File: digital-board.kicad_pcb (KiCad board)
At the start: 2 copper layers, 200 x 150 mm, 231 parts, among them IC1 ATMEGA6450-A, J1 CONN_20X2, Q1 2N3904, Q2 2N3904, SW15 TACT_SWITCH, SW16 TACT_SWITCH, SW17 TACT_SWITCH, SW18 TACT_SWITCH, SW19 TACT_SWITCH, SW20 TACT_SWITCH, SW21 TACT_SWITCH, SW22 TACT_SWITCH, SW23 TACT_SWITCH, U1 DG419, U10 74LVC1G32, U12 74AC595, U13 74AC595, U14 74HC165, U15 74AC595, U16 74AC595, U2 74HC4067, U3 R-78E5.0-1.0, U4 74HC4067, U5 74LS573, U6 74LS573, U7 74LVC2G04, U8 74AC595, U9 74HC165, X1 MIDI OUT, X2 MIDI IN, X3 MIDI THRU

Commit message: main routing done. touch ups, adding decoupling
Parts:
- removed LED1: LED, synth:LED-0805-JRL
- removed R4: 330, synth:SM0603-JRL
- added C18: 0.1µ, synth:SM0603-JRL, B.Cu at (94.5, 54.5)
- added C23: 0.1µ, synth:SM0603-JRL, B.Cu at (139.5, 54.5)
- added C24: 0.1µ, synth:SM0603-JRL, B.Cu at (114.5, 54.5)
- added C25: 0.1µ, synth:SM0603-JRL, B.Cu at (15.0, 83.5)
- added C26: 0.1µ, synth:SM0603-JRL, B.Cu at (47.5, 135.5)
- C7: moved to B.Cu
- moved C7 6.40 mm to (15.0, 43.5), turned to 270 degrees
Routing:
- net +5V: track 1728.5 -> 1822.5 mm, vias 13 -> 14
- net GND: track 293.6 -> 319.2 mm, vias 18 -> 22
- net Net-(U13-Pad9): track 132.9 -> 136.1 mm
- net DB2: track 349.1 -> 346.3 mm
- net Net-(LED1-Pad1): track 2.10 -> 0.00 mm
- net Net-(R49-Pad2): track 139.8 -> 141.5 mm
- net ~RESET: track 36.6 -> 35.3 mm
- net EG2 POL: track 145.9 -> 144.9 mm
- net SPI_SCK: track 272.7 -> 273.5 mm

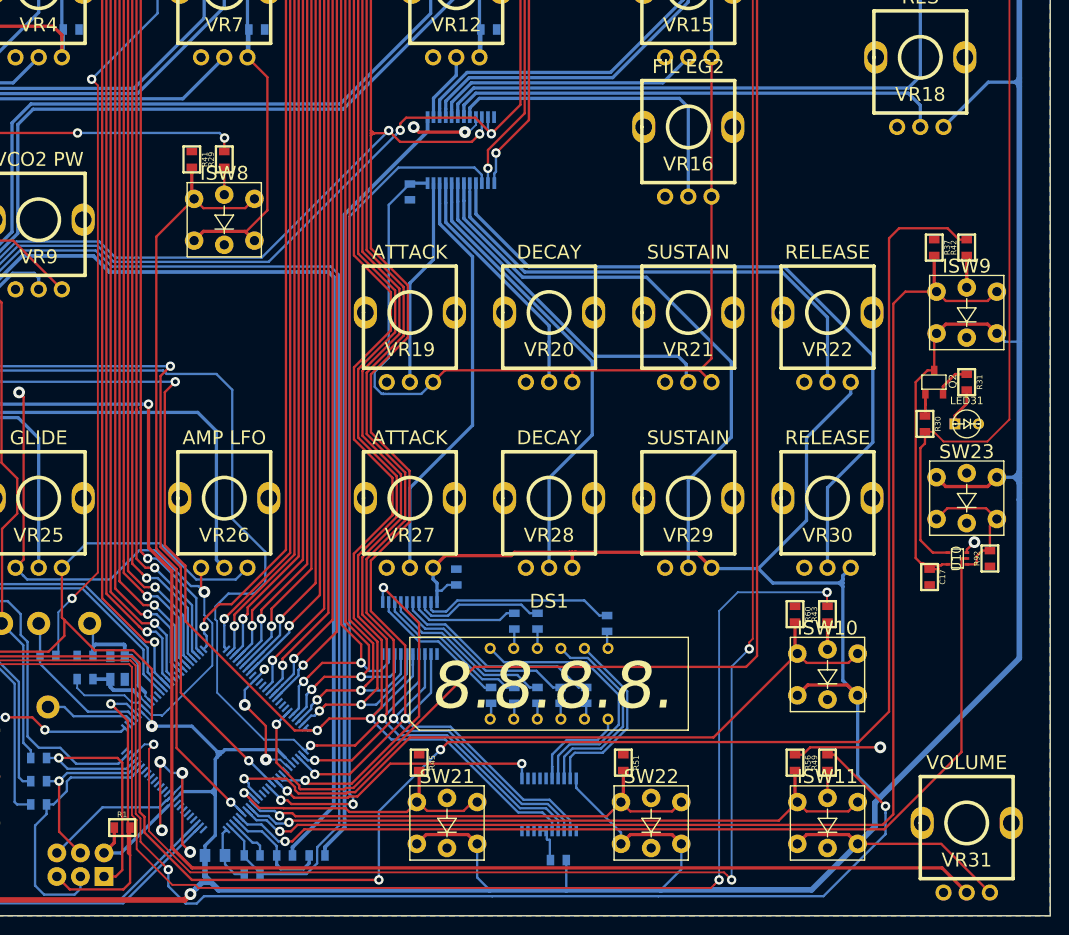
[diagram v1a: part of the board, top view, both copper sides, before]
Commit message: touching up +5V power rail tracks
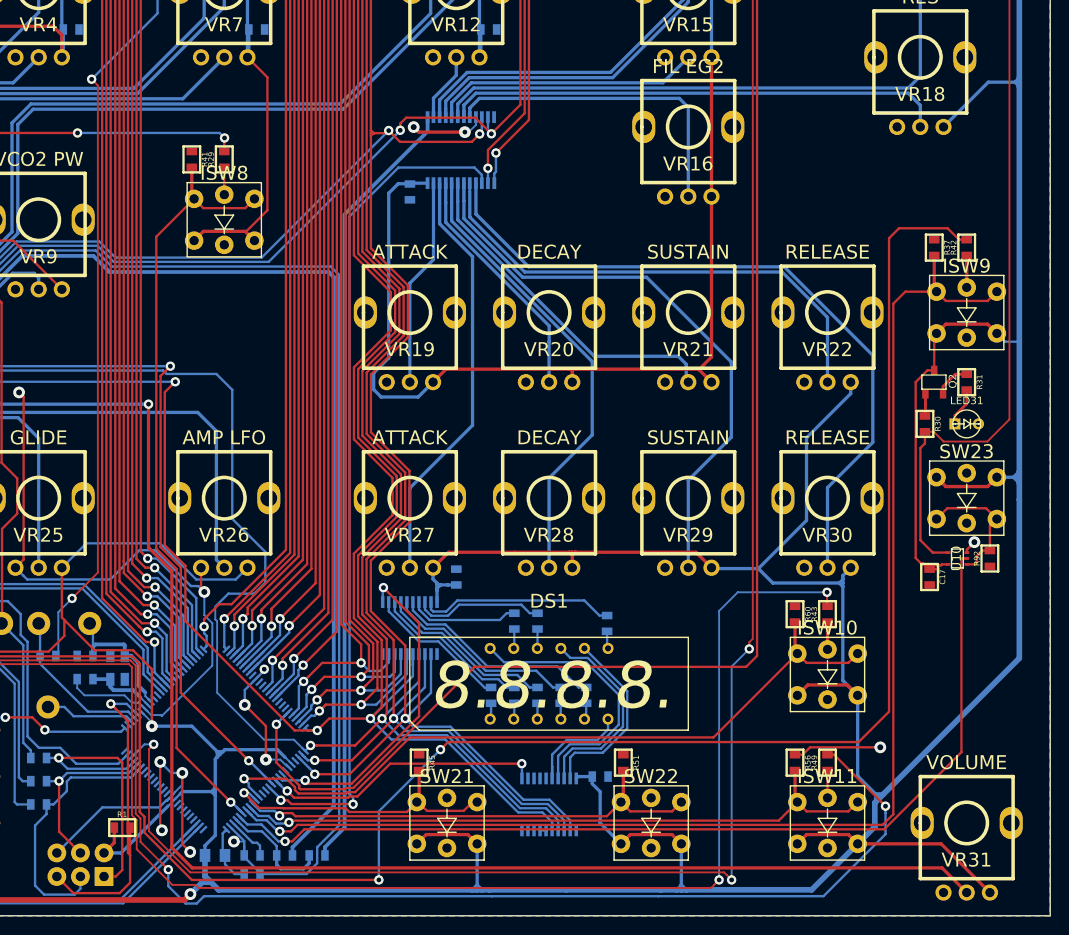
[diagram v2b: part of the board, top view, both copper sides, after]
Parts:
- moved C11 10.1 mm to (151.5, 135.0), turned to 0 degrees
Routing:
- net +5V: track 1822.5 -> 1830.1 mm
- net GND: track 319.2 -> 319.4 mm, vias 22 -> 23

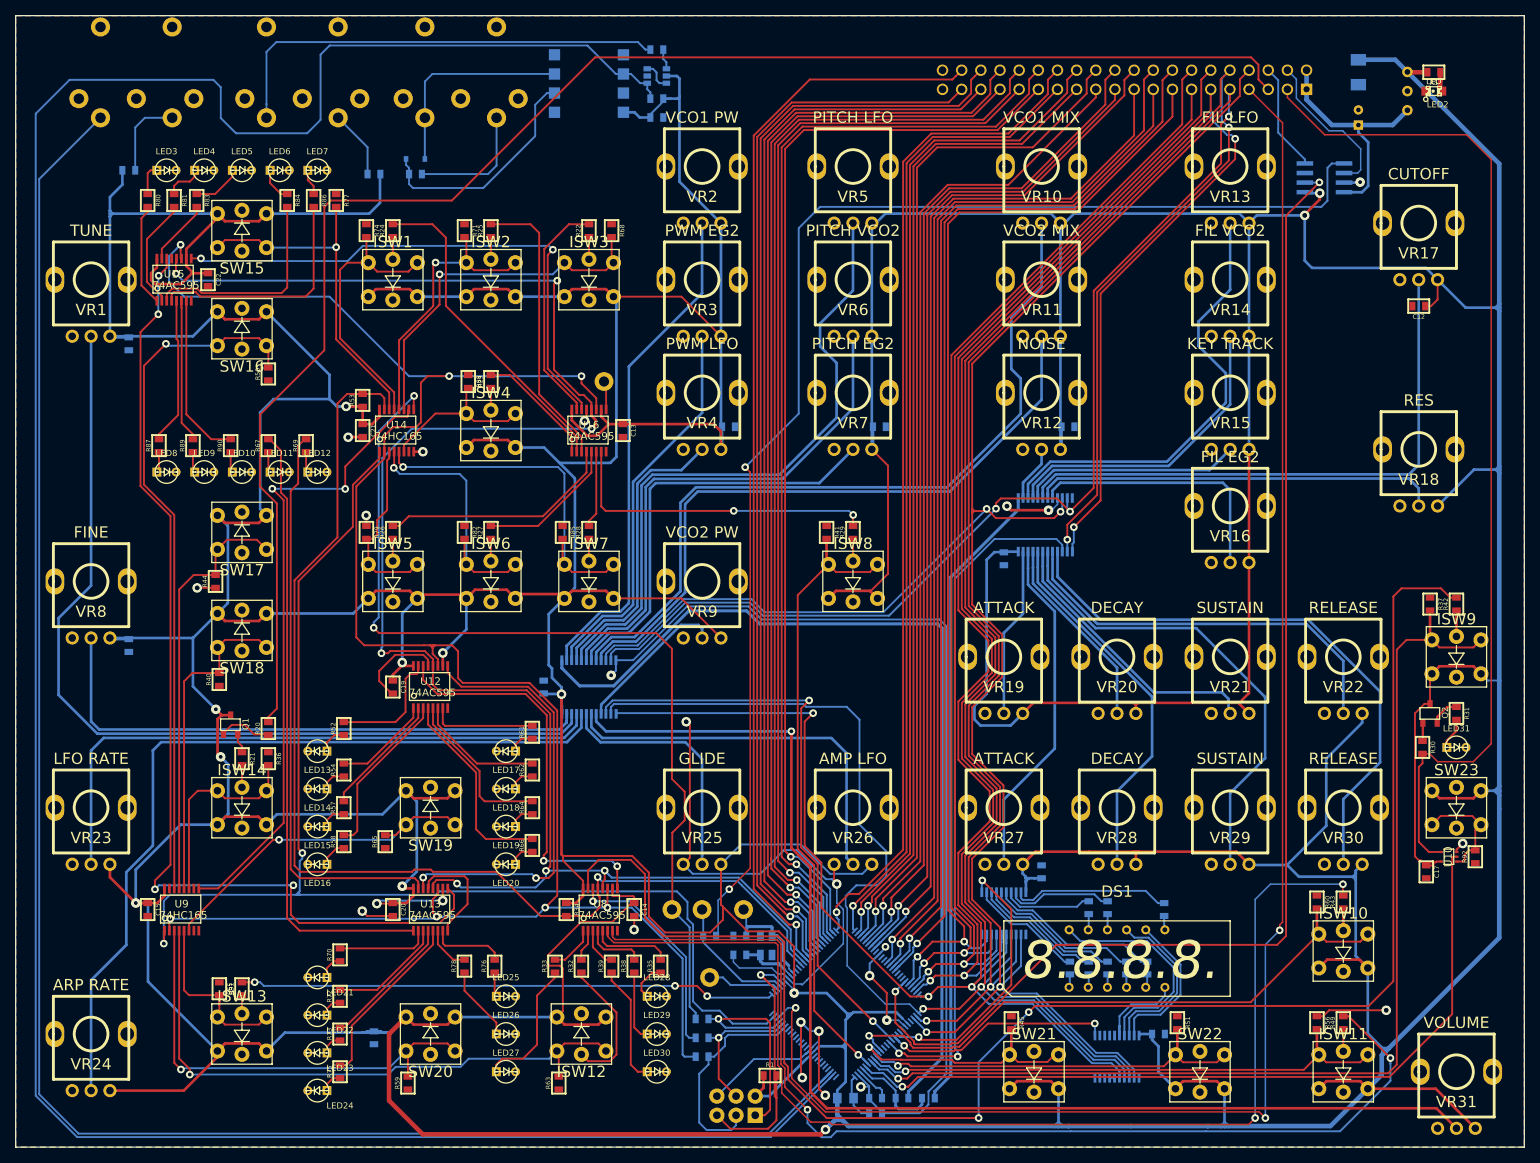
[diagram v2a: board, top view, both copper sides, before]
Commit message: added more decoupling caps and mounting holes
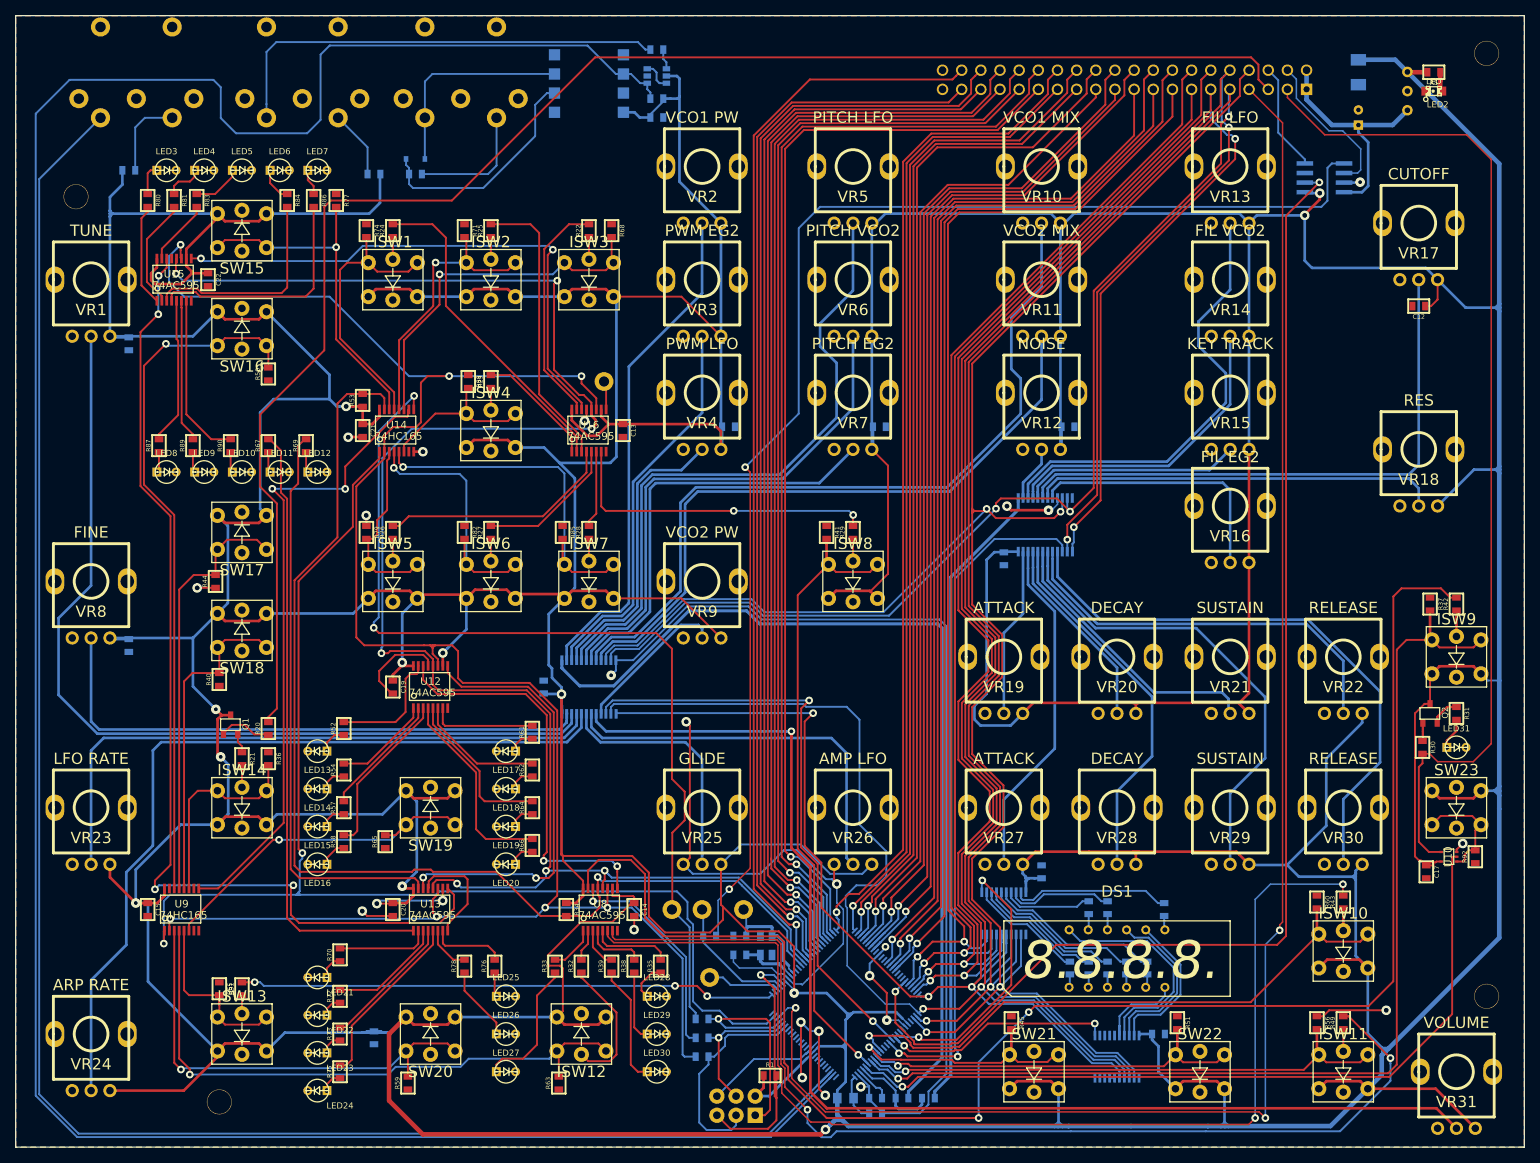
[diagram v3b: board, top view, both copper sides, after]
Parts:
- added HOLE-0.125-INCH: VAL**, MyModules:HOLE-0.125-INCH, F.Cu at (195.0, 5.00)
- added HOLE-0.125-INCH: VAL**, MyModules:HOLE-0.125-INCH, F.Cu at (195.0, 130.0)
- added HOLE-0.125-INCH: VAL**, MyModules:HOLE-0.125-INCH, F.Cu at (27.0, 144.0)
- added HOLE-0.125-INCH: VAL**, MyModules:HOLE-0.125-INCH, F.Cu at (8.00, 24.0)
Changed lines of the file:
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@@
     (tracks 3386)
     (zones 0)
-    (modules 234)
+    (modules 238)
     (nets 275)
   )
@@
     (mod_text_size 1.5 1.5)
     (mod_text_width 0.15)
-    (pad_size 2 2)
-    (pad_drill 1)
+    (pad_size 3.302 3.302)
+    (pad_drill 3.175)
     (pad_to_mask_clearance 0.2)
     (aux_axis_origin 0 0)
@@
     )
   )
+  (module MyModules:HOLE-0.125-INCH (layer F.Cu)
+    (at 195 5)
+    (fp_text reference HOLE-0.125-INCH (at 0 -5) (layer F.SilkS) hide
+      (effects (font (size 1.5 1.5) (thickness 0.15)))
+    )
+    (fp_text value VAL** (at 0 5) (layer F.SilkS) hide
+      (effects (font (size 1.5 1.5) (thickness 0.15)))
+    )
+    (pad "" thru_hole circle (at 0 0) (size 3.302 3.302) (drill 3.175) (layers *.Cu *.Mask F.SilkS)
+      (clearance 1.27))
+  )
+  (module MyModules:HOLE-0.125-INCH (layer F.Cu)
+    (at 195 130)
+    (fp_text reference HOLE-0.125-INCH (at 0 -5) (layer F.SilkS) hide
+      (effects (font (size 1.5 1.5) (thickness 0.15)))
+    )
+    (fp_text value VAL** (at 0 5) (layer F.SilkS) hide
+      (effects (font (size 1.5 1.5) (thickness 0.15)))
+    )
+    (pad "" thru_hole circle (at 0 0) (size 3.302 3.302) (drill 3.175) (layers *.Cu *.Mask F.SilkS)
+      (clearance 1.27))
+  )
+  (module MyModules:HOLE-0.125-INCH (layer F.Cu)
+    (at 27 144)
+    (fp_text reference HOLE-0.125-INCH (at 0 -5) (layer F.SilkS) hide
+      (effects (font (size 1.5 1.5) (thickness 0.15)))
+    )
+    (fp_text value VAL** (at 0 5) (layer F.SilkS) hide
+      (effects (font (size 1.5 1.5) (thickness 0.15)))
+    )
+    (pad "" thru_hole circle (at 0 0) (size 3.302 3.302) (drill 3.175) (layers *.Cu *.Mask F.SilkS)
+      (clearance 1.27))
+  )
+  (module MyModules:HOLE-0.125-INCH (layer F.Cu)
+    (at 8 24)
+    (fp_text reference HOLE-0.125-INCH (at 0 -5) (layer F.SilkS) hide
+      (effects (font (size 1.5 1.5) (thickness 0.15)))
+    )
+    (fp_text value VAL** (at 0 5) (layer F.SilkS) hide
+      (effects (font (size 1.5 1.5) (thickness 0.15)))
+    )
+    (pad "" thru_hole circle (at 0 0) (size 3.302 3.302) (drill 3.175) (layers *.Cu *.Mask F.SilkS)
+      (clearance 1.27))
+  )
   (gr_line (start 0 150) (end 0 0) (angle 90) (layer Edge.Cuts) (width 0.15))

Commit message: next step: footprint testing and silkscreen
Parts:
- moved HOLE-0.125-INCH 28.7 mm to (8.50, 122.0)
- moved HOLE-0.125-INCH 0.50 mm to (195.0, 130.5)
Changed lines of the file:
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@@
+  )
+  (module MyModules:HOLE-0.125-INCH (layer F.Cu)
+    (at 8 24)
+    (fp_text reference HOLE-0.125-INCH (at 0 -5) (layer F.SilkS) hide
+      (effects (font (size 1.5 1.5) (thickness 0.15)))
+    )
+    (fp_text value VAL** (at 0 5) (layer F.SilkS) hide
+      (effects (font (size 1.5 1.5) (thickness 0.15)))
+    )
+    (pad "" thru_hole circle (at 0 0) (size 3.302 3.302) (drill 3.175) (layers *.Cu *.Mask F.SilkS)
+      (clearance 1.905))
+  )
+  (module MyModules:HOLE-0.125-INCH (layer F.Cu)
+    (at 8.5 122)
+    (fp_text reference HOLE-0.125-INCH (at 0 -5) (layer F.SilkS) hide
+      (effects (font (size 1.5 1.5) (thickness 0.15)))
+    )
+    (fp_text value VAL** (at 0 5) (layer F.SilkS) hide
+      (effects (font (size 1.5 1.5) (thickness 0.15)))
+    )
+    (pad "" thru_hole circle (at 0 0) (size 3.302 3.302) (drill 3.175) (layers *.Cu *.Mask F.SilkS)
+      (clearance 1.905))
+  )
+  (module MyModules:HOLE-0.125-INCH (layer F.Cu)
+    (at 195 130.5)
+    (fp_text reference HOLE-0.125-INCH (at 0 -5) (layer F.SilkS) hide
+      (effects (font (size 1.5 1.5) (thickness 0.15)))
+    )
+    (fp_text value VAL** (at 0 5) (layer F.SilkS) hide
+      (effects (font (size 1.5 1.5) (thickness 0.15)))
+    )
+    (pad "" thru_hole circle (at 0 0) (size 3.302 3.302) (drill 3.175) (layers *.Cu *.Mask F.SilkS)
+      (clearance 1.905))
   )
   (module MyModules:HOLE-0.125-INCH (layer F.Cu)
@@
     )
     (pad "" thru_hole circle (at 0 0) (size 3.302 3.302) (drill 3.175) (layers *.Cu *.Mask F.SilkS)
-      (clearance 1.27))
-  )
-  (module MyModules:HOLE-0.125-INCH (layer F.Cu)
-    (at 195 130)
-    (fp_text reference HOLE-0.125-INCH (at 0 -5) (layer F.SilkS) hide
-      (effects (font (size 1.5 1.5) (thickness 0.15)))
-    )
-    (fp_text value VAL** (at 0 5) (layer F.SilkS) hide
-      (effects (font (size 1.5 1.5) (thickness 0.15)))
-    )
-    (pad "" thru_hole circle (at 0 0) (size 3.302 3.302) (drill 3.175) (layers *.Cu *.Mask F.SilkS)
-      (clearance 1.27))
-  )
-  (module MyModules:HOLE-0.125-INCH (layer F.Cu)
-    (at 27 144)
-    (fp_text reference HOLE-0.125-INCH (at 0 -5) (layer F.SilkS) hide
-      (effects (font (size 1.5 1.5) (thickness 0.15)))
-    )
-    (fp_text value VAL** (at 0 5) (layer F.SilkS) hide
-      (effects (font (size 1.5 1.5) (thickness 0.15)))
-    )
-    (pad "" thru_hole circle (at 0 0) (size 3.302 3.302) (drill 3.175) (layers *.Cu *.Mask F.SilkS)
-      (clearance 1.27))
-  )
-  (module MyModules:HOLE-0.125-INCH (layer F.Cu)
-    (at 8 24)
-    (fp_text reference HOLE-0.125-INCH (at 0 -5) (layer F.SilkS) hide
-      (effects (font (size 1.5 1.5) (thickness 0.15)))
-    )
-    (fp_text value VAL** (at 0 5) (layer F.SilkS) hide
-      (effects (font (size 1.5 1.5) (thickness 0.15)))
-    )
-    (pad "" thru_hole circle (at 0 0) (size 3.302 3.302) (drill 3.175) (layers *.Cu *.Mask F.SilkS)
-      (clearance 1.27))
+      (clearance 1.905))
   )
   (gr_line (start 0 150) (end 0 0) (angle 90) (layer Edge.Cuts) (width 0.15))

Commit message: last save before silk screen edit in 5112
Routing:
- net +5V: track 1830.1 -> 1830.7 mm
